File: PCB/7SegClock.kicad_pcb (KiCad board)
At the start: 2 copper layers, 177.8 x 76.2 mm, 40 parts, among them CON1 USB-MINI-B, Q1 NPN, U1 P8X32A, U2 24LC256, U3 FT232RL, U4 DS3231, U5 TPS62172DSGT, U6 LCMX02-640UHC-4TG144C, X1 5mhz CRYSTAL

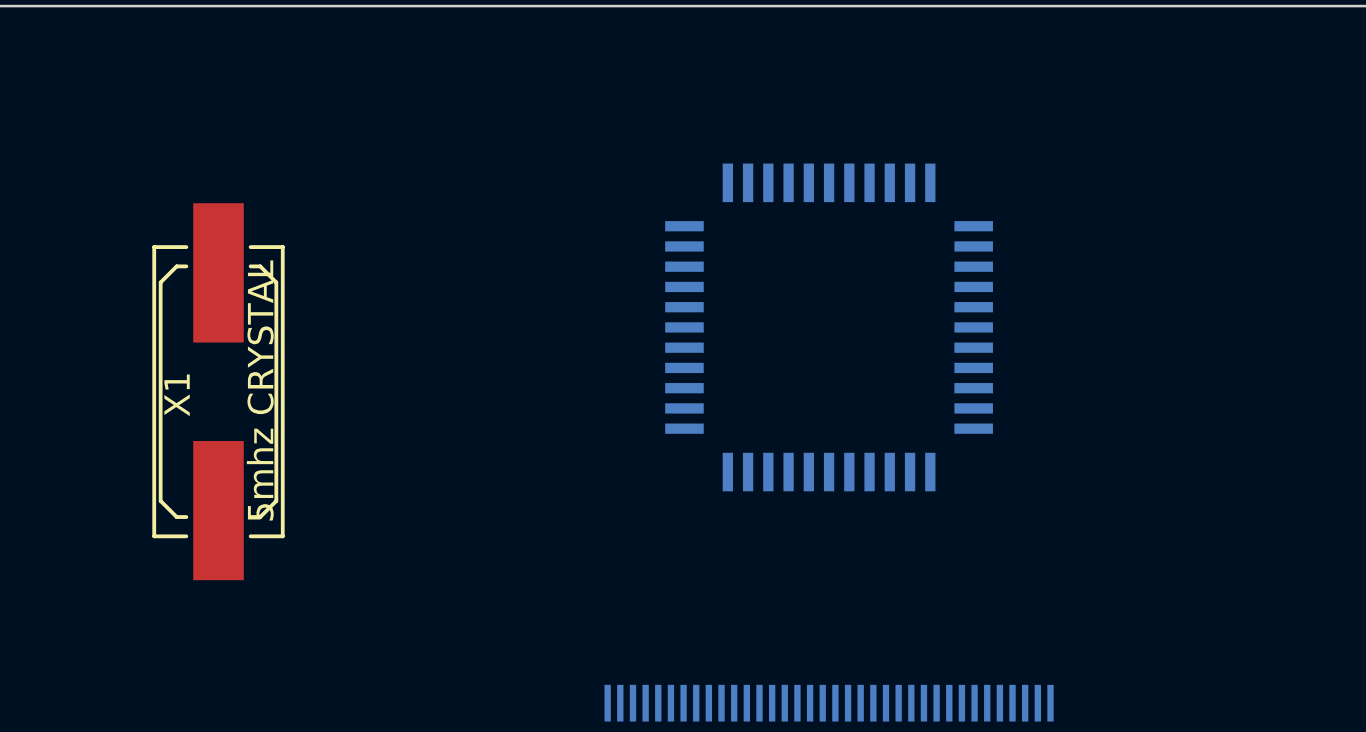
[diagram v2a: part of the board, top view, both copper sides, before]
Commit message: Worked on LED array.
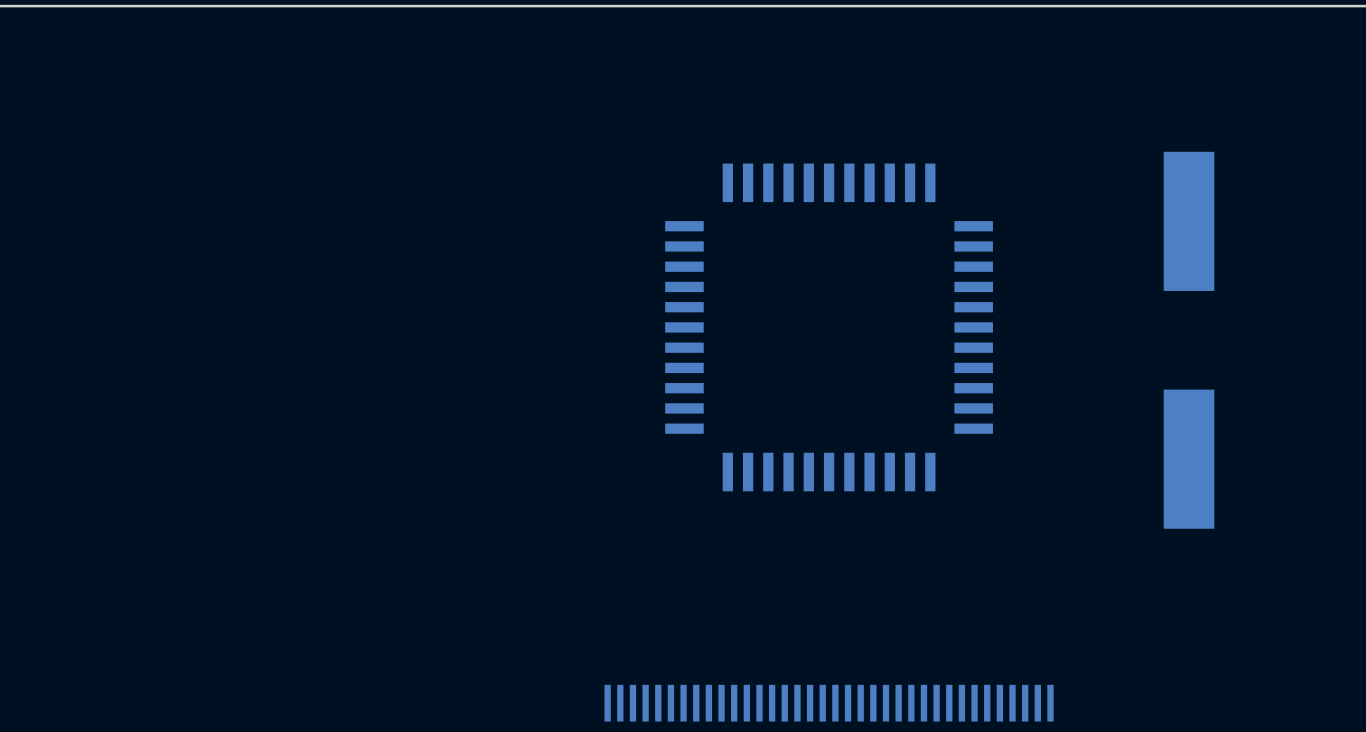
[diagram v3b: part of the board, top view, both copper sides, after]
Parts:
- X1: moved to B.Cu
- moved X1 38.4 mm to (164.1, 61.5), turned to 270 degrees
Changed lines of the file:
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@@
       (net 75 "Net-(U5-Pad4)"))
   )
-  (module Crystals_Oscillators_SMD:Q_49U3HMS (layer F.Cu)
-    (at 125.73 63.5 90)
-    (fp_text reference X1 (at -0.1 -1.6 90) (layer F.SilkS)
-      (effects (font (size 1 1) (thickness 0.15)))
+  (module Crystals_Oscillators_SMD:Q_49U3HMS (layer B.Cu)
+    (at 164.084 61.468 270)
+    (fp_text reference X1 (at -0.1 1.6 270) (layer B.SilkS)
+      (effects (font (size 1 1) (thickness 0.15)) (justify mirror))
     )
-    (fp_text value "5mhz CRYSTAL" (at 0 1.7 90) (layer F.SilkS)
-      (effects (font (size 1 1) (thickness 0.15)))
+    (fp_text value "5mhz CRYSTAL" (at 0 -1.7 270) (layer B.SilkS)
+      (effects (font (size 1 1) (thickness 0.15)) (justify mirror))
     )
-    (fp_line (start -4.953 -1.651) (end -4.953 -1.27) (layer F.SilkS) (width 0.15))
-    (fp_line (start -4.953 1.651) (end -4.953 1.27) (layer F.SilkS) (width 0.15))
-    (fp_line (start 4.953 1.651) (end 4.953 1.27) (layer F.SilkS) (width 0.15))
-    (fp_line (start 4.953 -1.651) (end 4.953 -1.27) (layer F.SilkS) (width 0.15))
-    (fp_line (start 5.715 -2.54) (end 5.715 -1.27) (layer F.SilkS) (width 0.15))
-    (fp_line (start 5.715 2.54) (end 5.715 1.27) (layer F.SilkS) (width 0.15))
-    (fp_line (start -5.715 2.54) (end -5.715 1.27) (layer F.SilkS) (width 0.15))
-    (fp_line (start -5.715 -2.54) (end -5.715 -1.27) (layer F.SilkS) (width 0.15))
-    (fp_line (start -4.953 1.651) (end -4.318 2.286) (layer F.SilkS) (width 0.15))
-    (fp_line (start -4.318 2.286) (end 4.318 2.286) (layer F.SilkS) (width 0.15))
-    (fp_line (start 4.318 2.286) (end 4.953 1.651) (layer F.SilkS) (width 0.15))
-    (fp_line (start 4.953 -1.651) (end 4.318 -2.286) (layer F.SilkS) (width 0.15))
-    (fp_line (start 4.318 -2.286) (end -4.318 -2.286) (layer F.SilkS) (width 0.15))
-    (fp_line (start -4.318 -2.286) (end -4.953 -1.651) (layer F.SilkS) (width 0.15))
-    (fp_line (start 5.715 2.54) (end -5.715 2.54) (layer F.SilkS) (width 0.15))
-    (fp_line (start -5.715 -2.54) (end 5.715 -2.54) (layer F.SilkS) (width 0.15))
-    (pad 1 smd rect (at -4.699 0 90) (size 5.4991 1.99898) (layers F.Cu F.Paste F.Mask)
+    (fp_line (start -4.953 1.651) (end -4.953 1.27) (layer B.SilkS) (width 0.15))
+    (fp_line (start -4.953 -1.651) (end -4.953 -1.27) (layer B.SilkS) (width 0.15))
+    (fp_line (start 4.953 -1.651) (end 4.953 -1.27) (layer B.SilkS) (width 0.15))
+    (fp_line (start 4.953 1.651) (end 4.953 1.27) (layer B.SilkS) (width 0.15))
+    (fp_line (start 5.715 2.54) (end 5.715 1.27) (layer B.SilkS) (width 0.15))
+    (fp_line (start 5.715 -2.54) (end 5.715 -1.27) (layer B.SilkS) (width 0.15))
+    (fp_line (start -5.715 -2.54) (end -5.715 -1.27) (layer B.SilkS) (width 0.15))
+    (fp_line (start -5.715 2.54) (end -5.715 1.27) (layer B.SilkS) (width 0.15))
+    (fp_line (start -4.953 -1.651) (end -4.318 -2.286) (layer B.SilkS) (width 0.15))
+    (fp_line (start -4.318 -2.286) (end 4.318 -2.286) (layer B.SilkS) (width 0.15))
+    (fp_line (start 4.318 -2.286) (end 4.953 -1.651) (layer B.SilkS) (width 0.15))
+    (fp_line (start 4.953 1.651) (end 4.318 2.286) (layer B.SilkS) (width 0.15))
+    (fp_line (start 4.318 2.286) (end -4.318 2.286) (layer B.SilkS) (width 0.15))
+    (fp_line (start -4.318 2.286) (end -4.953 1.651) (layer B.SilkS) (width 0.15))
+    (fp_line (start 5.715 -2.54) (end -5.715 -2.54) (layer B.SilkS) (width 0.15))
+    (fp_line (start -5.715 2.54) (end 5.715 2.54) (layer B.SilkS) (width 0.15))
+    (pad 1 smd rect (at -4.699 0 270) (size 5.4991 1.99898) (layers B.Cu B.Paste B.Mask)
       (net 28 "Net-(U1-Pad28)"))
-    (pad 2 smd rect (at 4.699 0 90) (size 5.4991 1.99898) (layers F.Cu F.Paste F.Mask)
+    (pad 2 smd rect (at 4.699 0 270) (size 5.4991 1.99898) (layers B.Cu B.Paste B.Mask)
       (net 34 "Net-(U1-Pad29)"))
     (model Crystals_Oscillators_SMD/Q_49U3HMS.wrl

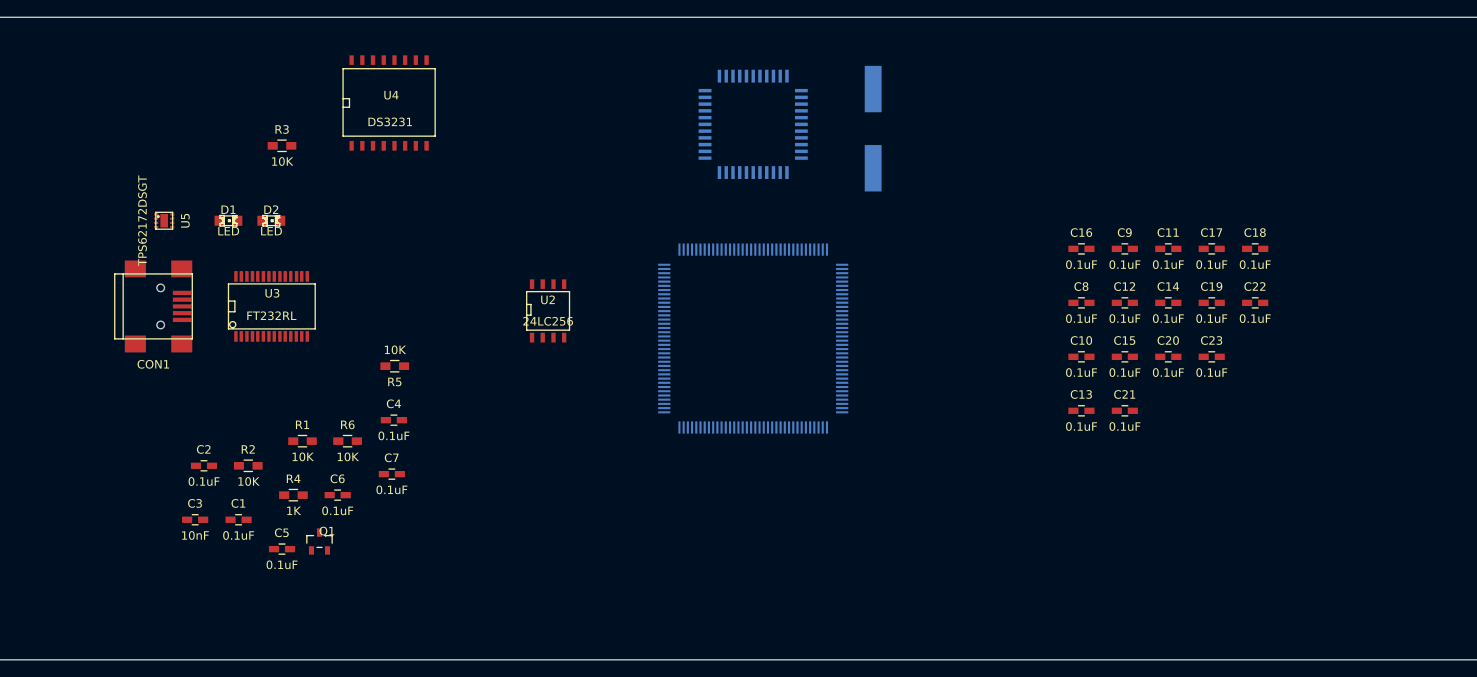
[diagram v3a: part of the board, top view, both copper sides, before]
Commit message: Finished LED array footprint.
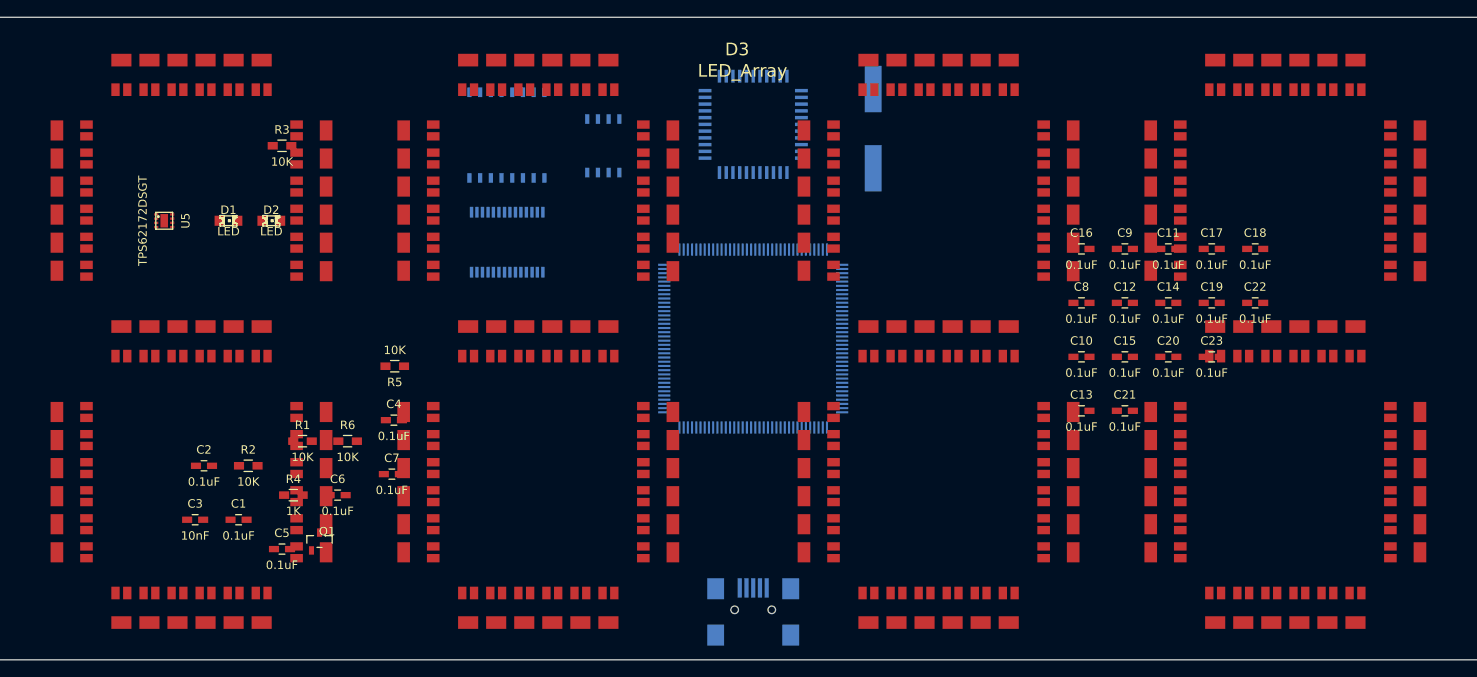
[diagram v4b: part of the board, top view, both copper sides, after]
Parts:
- added D3: LED_Array, Custom:LED-ARRAY, F.Cu at (74.9, 53.3)
- CON1, U2, U3, U4: moved to B.Cu
- moved CON1 80.1 mm to (149.9, 119.4), turned to 90 degrees
- moved U3 29.0 mm to (120.7, 74.9)
- moved U2 20.6 mm to (132.1, 63.5)
- moved U4 14.5 mm to (120.7, 62.2)

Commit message: Worked on PCB.
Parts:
- moved U5 83.9 mm to (148.6, 120.7)
- moved D3 80.7 mm to (148.6, 86.4)
- moved C1 75.0 mm to (119.3, 39.3)
- moved C3 75.0 mm to (114.2, 39.3)
- moved C6 75.0 mm to (131.1, 36.3)
- moved Q1 75.0 mm to (128.9, 41.8)
- moved R4 75.0 mm to (125.8, 36.3)
- moved C2 75.0 mm to (115.2, 32.9)
- moved C4 75.0 mm to (137.7, 27.5)
- moved R1 75.0 mm to (126.9, 29.9)
- moved R2 75.0 mm to (120.5, 32.9)
- moved R5 75.0 mm to (137.8, 21.1)
- moved R6 75.0 mm to (132.2, 29.9)
- moved C5 75.0 mm to (124.5, 42.7)
- moved C7 75.0 mm to (137.5, 33.9)
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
